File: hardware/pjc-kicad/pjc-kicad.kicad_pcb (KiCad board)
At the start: 2 copper layers, 0 parts

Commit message: Began laying out board
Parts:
- added C1: 10nF, SM1206_LP, F.Cu at (193.0, 233.7)
- added C10: 10uF, SM1206_LP, F.Cu at (429.3, 241.3)
- added C11: 1uF, SM1206_LP, F.Cu at (429.3, 254.0)
- added C12: 22pF, SM1206_LP, F.Cu at (314.3, 236.2)
- added C13: 22pF, SM1206_LP, F.Cu at (308.0, 236.2)
- added C14: 100nF, SM1206_LP, F.Cu at (350.5, 292.1)
- added C2: 100nF, SM1206_LP, F.Cu at (215.9, 233.7)
- added C3: 4.7uF, SM1206_LP, F.Cu at (221.0, 233.7)
- added C4: 100nF, SM1206_LP, F.Cu at (193.0, 256.5)
- added C5: 100nF, SM1206_LP, F.Cu at (233.7, 246.4)
- added C6: 100nF, SM1206_LP, F.Cu at (289.6, 292.1)
- added C7: 100nF, SM1206_LP, F.Cu at (322.6, 241.3)
- added C8: 100nF, SM1206_LP, F.Cu at (313.1, 273.7)
- added C9: 100nF, SM1206_LP, F.Cu at (318.1, 273.7)
- added CON1: USB-MINI-B, USB_MINI_B_LP, F.Cu at (182.9, 246.4)
- added CON10: CONN_2, MINI_CT_2_PTH, F.Cu at (254.0, 205.7)
- added CON2: CONN_3, MINI_CT_3_PTH, F.Cu at (373.4, 276.9)
- added CON3: CONN_2, JST_PH_2_PTH, F.Cu at (299.7, 315.0)
- added CON4: M023.5MM, SCREWTERM-3.5MM-2, F.Cu at (381.0, 205.7)
- added CON5: 4PIN_FAN_CONN, 4PIN_FAN_PTH, F.Cu at (332.7, 205.7)
- added CON6: CONN_2, MINI_CT_2_PTH, F.Cu at (309.9, 203.2)
- added CON7: CONN_2, MINI_CT_2_PTH, F.Cu at (292.1, 203.2)
- added CON8: AVR-ISP-10, AVR_ISP_PTH, F.Cu at (261.0, 260.4)
- added CON9: CONN_2, MINI_CT_2_PTH, F.Cu at (274.3, 203.2)
- added D1: S1M, SMA-DIODE_LP, F.Cu at (419.1, 243.8)
- added D2: Green, SM1206_DIODE_LP, F.Cu at (281.9, 241.3)
- added D3: Yellow, SM1206_DIODE_LP, F.Cu at (289.6, 241.3)
- added D4: Red, SM1206_DIODE_LP, F.Cu at (297.2, 241.3)
- added F1: 120mA, SM1206_LP, F.Cu at (462.3, 264.2)
- added F2: 120mA, SM1206_LP, F.Cu at (317.5, 203.2)
- added F3: 120mA, SM1206_LP, F.Cu at (299.7, 203.2)
- added F4: 120mA, SM1206_LP, F.Cu at (281.9, 203.2)
- added F5: 120mA, SM1206_LP, F.Cu at (261.6, 203.2)
- added JP1: JUMPER-2PTH, SparkFun-1X02, F.Cu at (320.0, 223.5)
- added L1: INDUCTOR_SMALL, SM1206_LP, F.Cu at (203.2, 236.2)
- added MH1: MNT_HOLE_NPT, MNT_HOLE_4x10mm, F.Cu at (61.0, 55.9)
- added MH2: MNT_HOLE_NPT, MNT_HOLE_4x10mm, F.Cu at (78.7, 55.9)
- added MH3: MNT_HOLE_NPT, MNT_HOLE_4x10mm, F.Cu at (61.0, 76.2)
- added MH4: MNT_HOLE_NPT, MNT_HOLE_4x10mm, F.Cu at (78.7, 76.2)
- added Q1: MOSFET_P, SOT23GDS_LP, F.Cu at (233.7, 238.8)
- added Q2: RSQ045N03, SOT23-6_LP, F.Cu at (383.5, 218.4)
- added R1: 3.3k, SM1206_LP, F.Cu at (360.7, 276.9)
- added R10: 10k, SM1206_LP, F.Cu at (348.0, 241.3)
- added R11: 470, SM1206_LP, F.Cu at (281.9, 228.6)
- added R12: 10k, SM1206_LP, F.Cu at (293.4, 271.8)
- added R13: 1.5k, SM1206_LP, F.Cu at (289.6, 228.6)
- added R14: 2.2k, SM1206_LP, F.Cu at (297.2, 228.6)
- added R15: 10k, SM1206_LP, F.Cu at (327.7, 226.1)
- added R16: 10k, SM1206_LP, F.Cu at (266.7, 231.1)
- added R17: 10k, SM1206_LP, F.Cu at (360.7, 238.8)
- added R18: 10k, SM1206_LP, F.Cu at (342.9, 226.1)
- added R19: 3.3k, SM1206_LP, F.Cu at (355.6, 226.1)
- added R2: 10k, SM1206_LP, F.Cu at (315.0, 304.8)
- added R3: 10k, SM1206_LP, F.Cu at (292.1, 302.3)
- added R4: 10k, SM1206_LP, F.Cu at (304.8, 307.3)
- added R5: 20k, SM1206_LP, F.Cu at (342.9, 261.6)
- added R6: 10k, SM1206_LP, F.Cu at (221.0, 248.9)
- added R7: 1k, SM1206_LP, F.Cu at (233.7, 251.5)
- added R8: 10k, SM1206_LP, F.Cu at (348.0, 248.9)
- added R9: 3.3k, SM1206_LP, F.Cu at (373.4, 215.9)
- added S1: TAC_SWITCHSMD, TACTILE-SW-PTH, F.Cu at (360.7, 254.0)
- added SW1: SWITCH_INV, SWITCH_SPDT_LP, F.Cu at (444.5, 264.2)
- added TP1: TST, PINTST, F.Cu at (210.8, 236.2)
- added TP10: TST, PINTST, F.Cu at (439.4, 256.5)
- added TP11: TST, PINTST, F.Cu at (469.9, 264.2)
- added TP12: TST, PINTST, F.Cu at (297.2, 248.9)
- added TP13: TST, PINTST, F.Cu at (289.6, 248.9)
- added TP14: TST, PINTST, F.Cu at (363.2, 302.3)
- added TP15: TST, PINTST, F.Cu at (281.9, 248.9)
- added TP16: TST, PINTST, F.Cu at (269.2, 226.1)
- added TP17: TST, PINTST, F.Cu at (325.1, 274.3)
- added TP2: TST, PINTST, F.Cu at (302.3, 302.3)
- added TP3: TST, PINTST, F.Cu at (330.2, 271.8)
- added TP4: TST, PINTST, F.Cu at (439.4, 271.8)
- added TP5: TST, PINTST, F.Cu at (302.3, 269.2)
- added TP8: TST, PINTST, F.Cu at (325.1, 251.5)
- added TP9: TST, PINTST, F.Cu at (322.6, 251.5)
- added U1: VOM618A-4T, SOP-4_LP, F.Cu at (345.4, 274.3)
- added U10: NUD3124, SOT23-6_LP, F.Cu at (269.2, 215.9)
- added U2: MCP3301, SOIC8_LP, F.Cu at (304.8, 294.6)
- added U3: FT232RL, SSOP28_LP, F.Cu at (208.3, 248.9)
- added U4: BSP762T, SOIC8_LP, F.Cu at (348.0, 215.9)
- added U5: ATMEGA328-P, DIP-28_SOCK, F.Cu at (317.5, 259.1)
- added U6: SN74LVC1G07, SOT23-5_LP, F.Cu at (330.2, 241.3)
- added U7: L78M05C, DPAK_VREG_LP, F.Cu at (440.1, 247.0)
- added U8: NUD3124, SOT23-6_LP, F.Cu at (292.1, 215.9)
- added U9: TMP36_SOIC, SOIC8_LP, F.Cu at (365.8, 294.6)
- added X1: 20MHz, XTAL_SMD, F.Cu at (311.1, 247.7)
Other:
- net class Default: via_drill 0.635 -> 0.508

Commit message: More work on layout
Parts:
- moved MH4 377.4 mm to (381.0, 302.3)
- moved MH2 334.0 mm to (378.5, 203.2)
- moved MH1 229.2 mm to (222.0, 218.9)
- moved MH3 229.2 mm to (222.0, 239.3)
- moved CON1 201.5 mm to (381.0, 283.2), turned to 180 degrees
- moved C1 189.6 mm to (372.1, 295.9), turned to 270 degrees
- moved L1 173.2 mm to (365.8, 295.9), turned to 270 degrees
- moved C4 169.1 mm to (359.4, 287.0)
- moved C2 158.0 mm to (359.4, 299.7), turned to 270 degrees
- moved TP1 153.3 mm to (353.1, 293.4), turned to 270 degrees
- moved U3 149.3 mm to (355.6, 273.1), turned to 270 degrees
- moved C3 147.7 mm to (353.1, 299.7), turned to 270 degrees
- moved Q1 142.6 mm to (372.1, 273.1), turned to 90 degrees
- moved C5 138.7 mm to (370.8, 266.7), turned to 0 degrees
- moved R6 137.5 mm to (353.1, 287.0), turned to 90 degrees
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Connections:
- R16 pad 1: /LED_EN_RED -> /LAMP_EN
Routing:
- net /LAMP_EN: track 0.00 -> 59.4 mm
- net /LED_EN_GREEN: track 0.00 -> 56.3 mm
- net /LED_EN_YELLOW: track 0.00 -> 50.6 mm
- net +5V: track 0.00 -> 47.8 mm
- net /LED_EN_RED: track 0.00 -> 46.1 mm
- net +12V: track 0.00 -> 35.7 mm
- net N-0000033: track 0.00 -> 32.3 mm
- net /FAN_PWM: track 0.00 -> 29.9 mm
- net N-0000071: track 0.00 -> 19.1 mm
- net N-0000072: track 0.00 -> 19.1 mm
- net /USB_VBUS: track 0.00 -> 15.0 mm
- net GND: track 0.00 -> 9.83 mm, vias 0 -> 2
- net N-000007: track 0.00 -> 8.69 mm
- net N-000006: track 0.00 -> 8.69 mm
- net N-000001: track 0.00 -> 8.69 mm
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
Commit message: Completed USB portion of layout
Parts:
- moved C4 18.2 mm to (367.0, 270.5)
- moved TP4 14.2 mm to (365.8, 260.4)
- moved Q1 8.52 mm to (379.7, 269.2), turned to 180 degrees
- moved C2 3.81 mm to (359.4, 295.9)
- moved C3 3.81 mm to (353.1, 295.9)
- moved TP1 3.81 mm to (353.1, 289.6)
- moved F1 3.81 mm to (355.6, 255.3)
- moved SW1 3.81 mm to (373.4, 255.3)
- moved TP11 3.81 mm to (348.0, 255.3)
- moved C5 3.59 mm to (373.4, 269.2), turned to 90 degrees
- moved R6 2.40 mm to (355.1, 285.8), turned to 0 degrees
- moved R7 0.51 mm to (367.0, 283.7)
- moved U3 0.25 mm to (355.3, 273.1), turned to 0 degrees
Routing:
- net /USB_VBUS: track 15.0 -> 91.0 mm, vias 0 -> 1
- net N-0000026: track 0.00 -> 29.6 mm
- net N-0000027: track 0.00 -> 28.4 mm
- net N-0000034: track 0.00 -> 19.7 mm
- net N-0000044: track 0.00 -> 19.0 mm
- net /~USB_PWREN: track 0.00 -> 18.8 mm
- net N-000004: track 0.00 -> 10.8 mm
- net +5V_USB: track 0.00 -> 6.58 mm

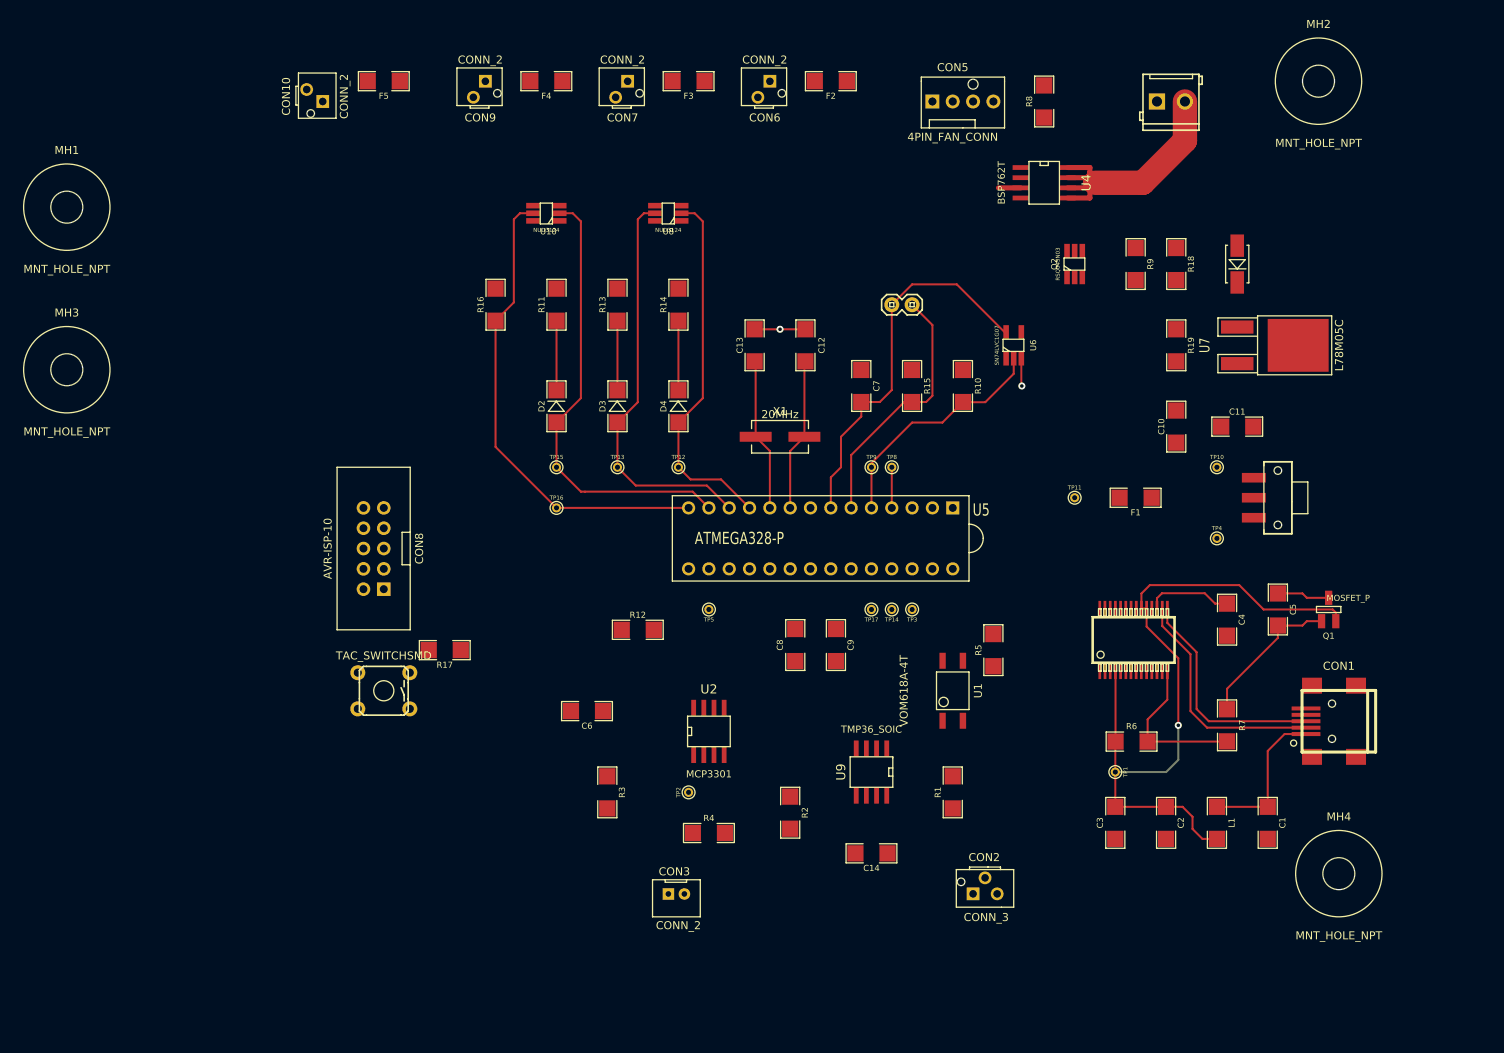
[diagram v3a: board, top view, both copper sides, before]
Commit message: Much closer to finished layout.
Redid decoupling caps so that both ends connect directly to IC devices.
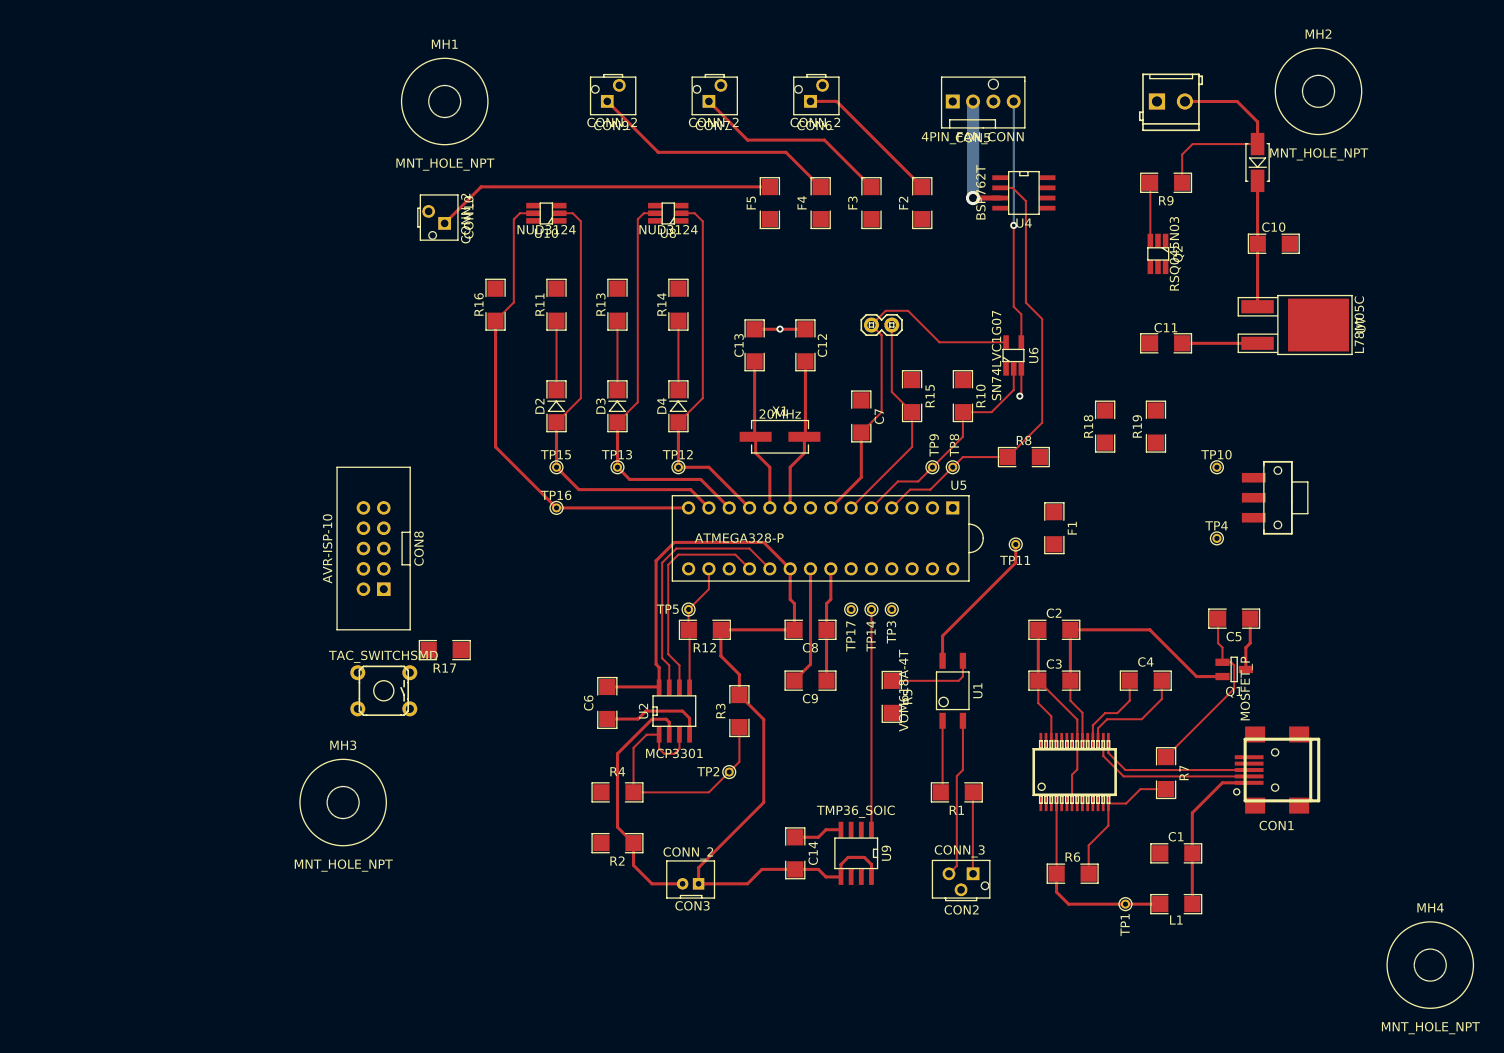
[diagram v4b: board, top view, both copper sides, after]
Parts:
- moved MH3 64.2 mm to (256.5, 293.4)
- moved F5 50.6 mm to (309.9, 218.4), turned to 90 degrees
- moved MH1 49.1 mm to (269.2, 205.7)
- moved R8 44.5 mm to (341.6, 250.2), turned to 0 degrees
- moved F4 37.5 mm to (316.2, 218.4), turned to 90 degrees
- moved C2 27.9 mm to (345.4, 271.8), turned to 180 degrees
- moved F3 27.5 mm to (322.6, 218.4), turned to 90 degrees
- moved C10 25.9 mm to (372.9, 223.5), turned to 0 degrees
- moved R18 22.2 mm to (351.8, 246.4)
- moved R2 21.9 mm to (290.8, 298.4), turned to 180 degrees
- moved CON10 21.6 mm to (269.2, 221.0)
- moved R3 19.4 mm to (306.1, 281.9)
- moved C3 19.3 mm to (345.4, 278.1), turned to 180 degrees
- moved F2 19.1 mm to (328.9, 218.4), turned to 90 degrees
- moved R6 18.1 mm to (347.7, 302.3)
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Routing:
- net +5V: track 47.8 -> 186.1 mm
- net GND: track 9.83 -> 86.4 mm
- net /FAN_EN: track 5.08 -> 55.6 mm
- net N-0000066: track 0.00 -> 42.6 mm
- net N-000008: track 0.00 -> 35.2 mm
- net N-0000015: track 0.00 -> 31.8 mm
- net /SCK: track 0.00 -> 31.2 mm
- net N-0000063: track 0.00 -> 31.1 mm
- net N-0000052: track 0.00 -> 30.5 mm, vias 0 -> 1
- net /USB_VBUS: track 91.0 -> 61.2 mm, vias 1 -> 0
- net /ANA_AMBIENT: track 0.00 -> 27.5 mm
- net /MISO: track 0.00 -> 27.3 mm
- net N-0000067: track 0.00 -> 24.8 mm
- net N-0000056: track 0.00 -> 19.8 mm
- net N-0000065: track 0.00 -> 18.4 mm
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
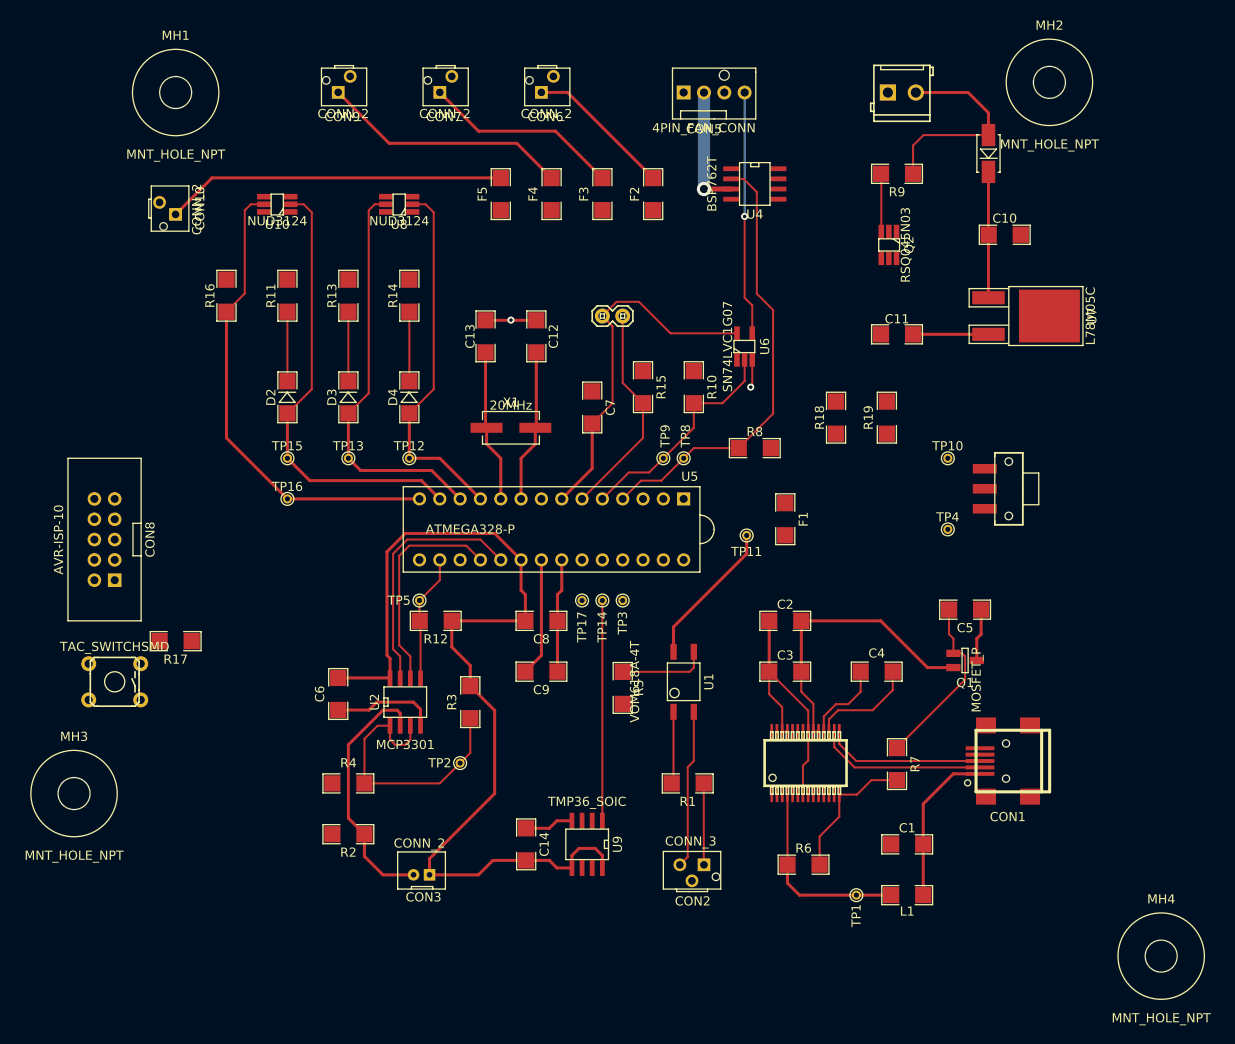
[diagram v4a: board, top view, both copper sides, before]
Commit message: More layout work.
Rearranged a couple of pieces to reduce space (still working on that) and wired up more areas, including the ISP connector.
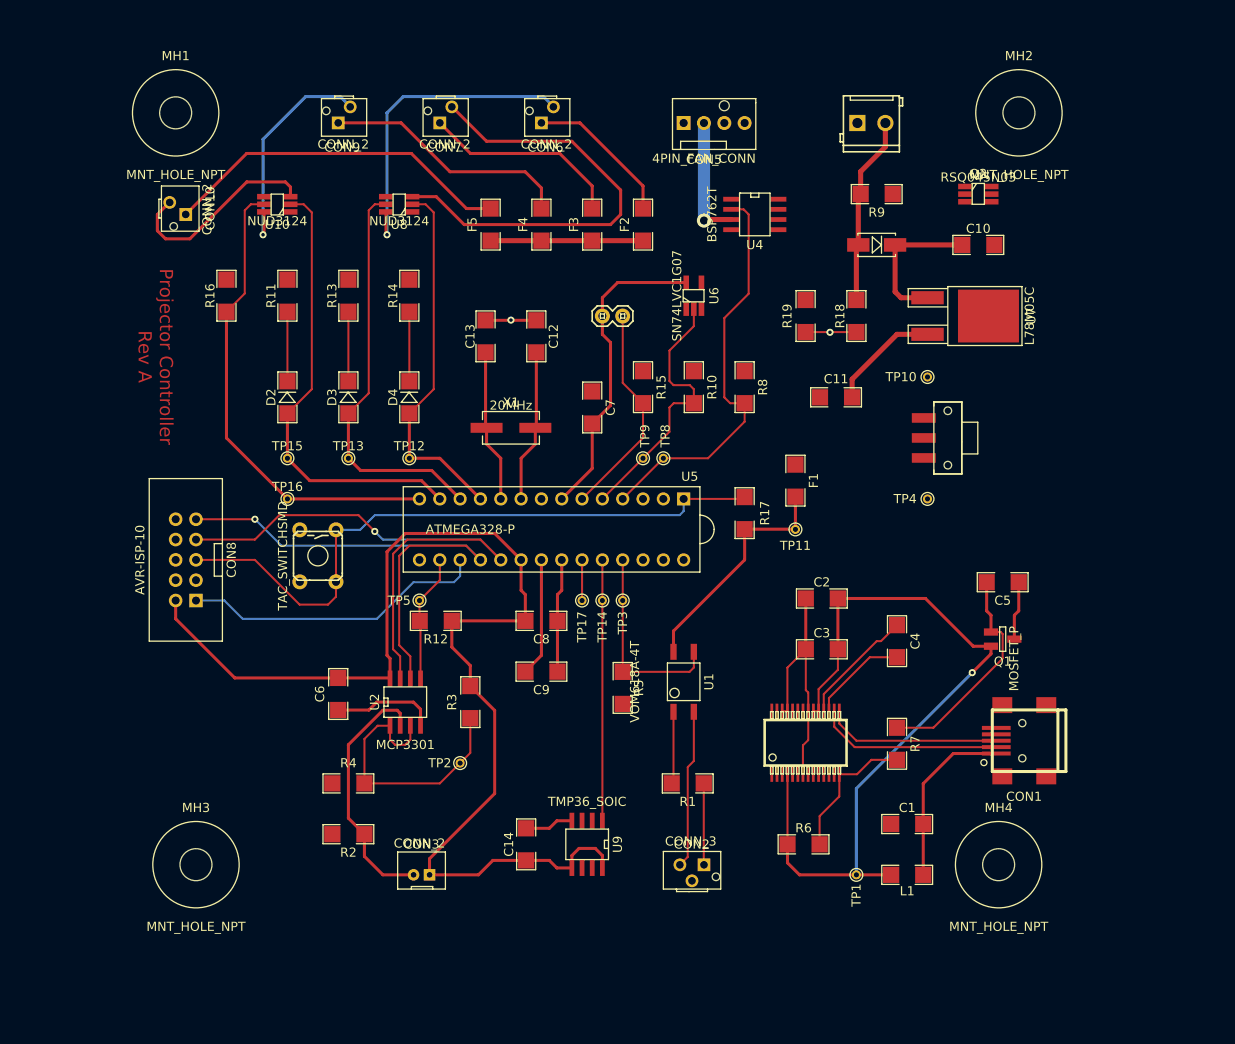
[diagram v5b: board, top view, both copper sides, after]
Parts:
- moved R17 72.9 mm to (340.4, 258.3), turned to 90 degrees
- moved S1 29.9 mm to (287.0, 263.7), turned to 270 degrees
- moved MH4 23.3 mm to (372.1, 302.3)
- moved D1 18.1 mm to (356.9, 224.8), turned to 0 degrees
- moved MH3 17.6 mm to (271.8, 302.3)
- moved R19 16.3 mm to (348.0, 233.7)
- moved R18 13.0 mm to (354.3, 233.7)
- moved Q2 12.9 mm to (369.6, 218.4), turned to 270 degrees
- moved C11 11.0 mm to (351.8, 243.8)
- moved TP10 10.5 mm to (363.2, 241.3)
- moved CON8 10.5 mm to (271.8, 264.2)
- moved SW1 9.92 mm to (365.8, 248.9)
- moved U6 8.98 mm to (334.0, 231.1)
- moved R8 7.73 mm to (340.4, 242.6), turned to 90 degrees
- moved U7 7.62 mm to (363.2, 233.7)
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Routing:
- net /~RESET: track 0.00 -> 82.2 mm
- net N-0000061: track 0.00 -> 56.5 mm
- net /SCK: track 31.2 -> 72.9 mm, vias 0 -> 1
- net N-0000059: track 0.00 -> 40.4 mm, vias 0 -> 1
- net /MOSI: track 0.00 -> 38.2 mm
- net /MISO: track 27.3 -> 65.0 mm, vias 0 -> 1
- net /USB_VBUS: track 61.2 -> 97.6 mm, vias 0 -> 1
- net +5V: track 186.1 -> 217.1 mm
- net N-0000052: track 30.5 -> 0.00 mm, vias 1 -> 0
- net N-0000060: track 0.00 -> 28.5 mm, vias 0 -> 1
- net N-0000062: track 0.00 -> 25.7 mm
- net +12V: track 26.4 -> 42.7 mm
- net /PROJECTOR_ON: track 11.1 -> 25.1 mm
- net /ANA_12V_FB: track 0.00 -> 11.5 mm, vias 0 -> 1
- net N-0000046: track 7.26 -> 0.00 mm
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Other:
- board text added: "Projector Controller Rev A"
